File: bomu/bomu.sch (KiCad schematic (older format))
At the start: 19 parts, among them U1 NRF52840-CKAA-R7

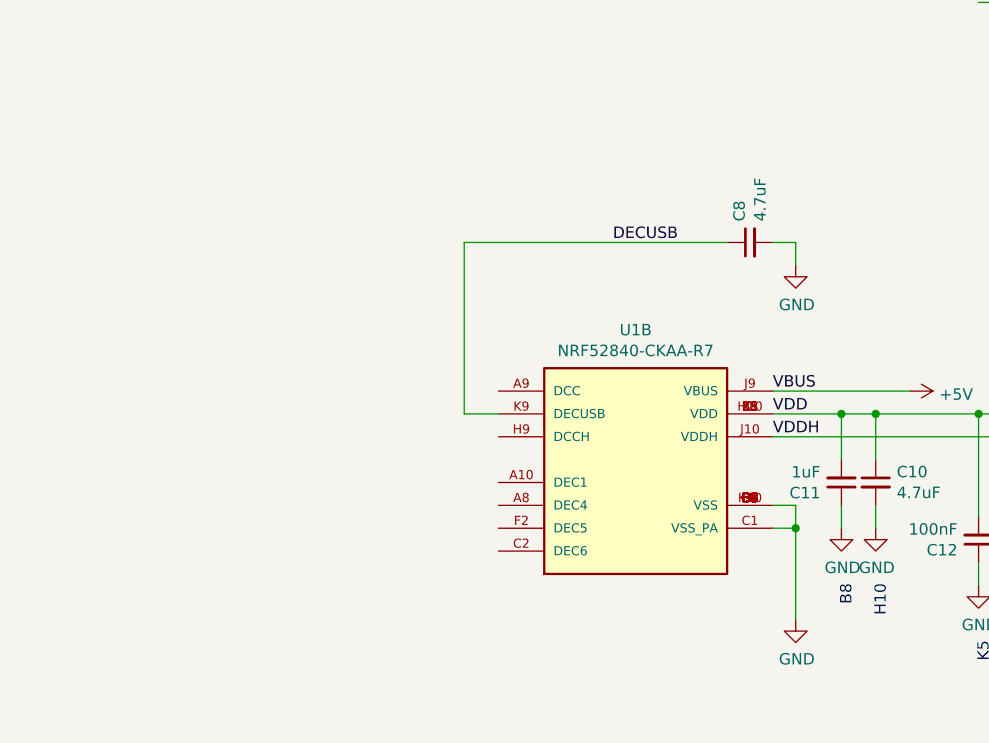
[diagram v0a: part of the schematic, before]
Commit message: Added remaining components to schematic
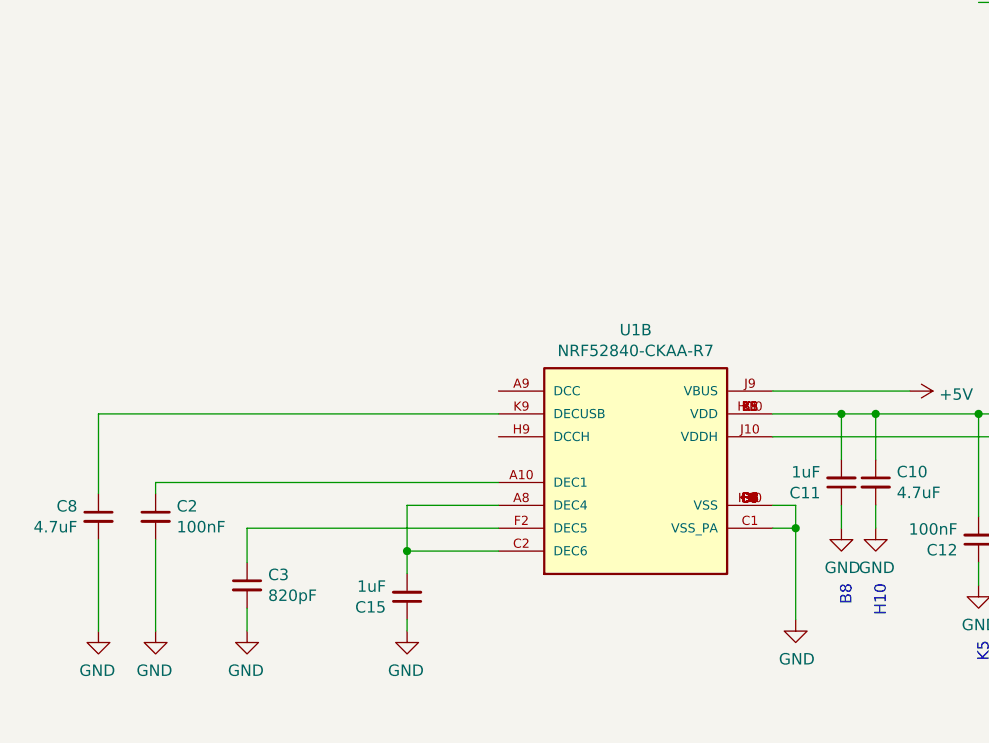
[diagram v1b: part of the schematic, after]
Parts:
- added C15: 1uF, Capacitor_SMD:C_0201_0603Metric, symbol Device:C_Small
- added C2: 100nF, Capacitor_SMD:C_0201_0603Metric, symbol Device:C_Small
- added C3: 820pF, Capacitor_SMD:C_0201_0603Metric, symbol Device:C_Small
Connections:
- net +5V: no longer R1.1
- net GND: now also C15.1, C2.2, C3.2
- net at U1.A10 (DEC1): now also C2.1
- net at U1.A8 (DEC4): now also U1.C2 (DEC6), C15.2
- net at U1.F2 (DEC5): now also C3.1
- net DECUSB: no longer names the net of C8.1, U1.K9 (DECUSB)
- new net VBUS: R1.1
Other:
- moved on the sheet: C8
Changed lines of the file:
@@
 	0    1    1    0
 $EndComp
-Text Label 3800 6300 0    50   ~ 0
-VBUS
-Text Label 3800 6400 0    50   ~ 0
-VDD
 $Comp
 L power:+3V0 #PWR?
@@
 	-1   0    0    1
 $EndComp
-Text Label 3800 6500 0    50   ~ 0
-VDDH
 $Comp
 L Device:R_Small_US R1
@@
 Wire Wire Line
 	3800 6400 4100 6400
-Text Label 3100 5650 0    50   ~ 0
-DECUSB
-$Comp
-L Device:C_Small C8
-U 1 1 5FCE36A5
-P 3700 5650
-F 0 "C8" H 3792 5696 50  0000 L CNN
-F 1 "4.7uF" H 3792 5605 50  0000 L CNN
-F 2 "Capacitor_SMD:C_0201_0603Metric" H 3700 5650 50  0001 C CNN
-F 3 "~" H 3700 5650 50  0001 C CNN
-	1    3700 5650
-	0    -1   -1   0
-$EndComp
-Wire Wire Line
-	3800 5650 3900 5650
-Wire Wire Line
-	3900 5650 3900 5750
 $Comp
 L power:GND #PWR?
 U 1 1 5FCE4C22
-P 3900 5750
-F 0 "#PWR?" H 3900 5500 50  0001 C CNN
-F 1 "GND" H 3905 5577 50  0000 C CNN
-F 2 "" H 3900 5750 50  0001 C CNN
-F 3 "" H 3900 5750 50  0001 C CNN
-	1    3900 5750
-	1    0    0    -1
-$EndComp
-Wire Wire Line
-	2600 6400 2450 6400
-Wire Wire Line
-	2450 6400 2450 5650
-Wire Wire Line
-	2450 5650 3600 5650
+P 850 7350
+F 0 "#PWR?" H 850 7100 50  0001 C CNN
+F 1 "GND" H 855 7177 50  0000 C CNN
+F 2 "" H 850 7350 50  0001 C CNN
+F 3 "" H 850 7350 50  0001 C CNN
+	1    850  7350
+	-1   0    0    -1
+$EndComp
 $Comp
 L Device:C_Small C10
@@
 Wire Wire Line
 	4150 2800 5100 2800
+$Comp
+L Device:C_Small C2
+U 1 1 5FE2FA10
+P 1100 6850
+F 0 "C2" H 1192 6896 50  0000 L CNN
+F 1 "100nF" H 1192 6805 50  0000 L CNN
+F 2 "Capacitor_SMD:C_0201_0603Metric" H 1100 6850 50  0001 C CNN
+F 3 "~" H 1100 6850 50  0001 C CNN
+	1    1100 6850
+	1    0    0    -1
+$EndComp
+$Comp
+L power:GND #PWR?
+U 1 1 5FE31818
+P 1100 7350
+F 0 "#PWR?" H 1100 7100 50  0001 C CNN
+F 1 "GND" H 1105 7177 50  0000 C CNN
+F 2 "" H 1100 7350 50  0001 C CNN
+F 3 "" H 1100 7350 50  0001 C CNN
+	1    1100 7350
+	-1   0    0    -1
+$EndComp
+Wire Wire Line
+	1100 7350 1100 6950
+Wire Wire Line
+	1100 6750 1100 6700
+Wire Wire Line
+	1100 6700 2600 6700
+$Comp
+L Device:C_Small C3
+U 1 1 5FE3522F
+P 1500 7150
+F 0 "C3" H 1592 7196 50  0000 L CNN
+F 1 "820pF" H 1592 7105 50  0000 L CNN
+F 2 "Capacitor_SMD:C_0201_0603Metric" H 1500 7150 50  0001 C CNN
+F 3 "~" H 1500 7150 50  0001 C CNN
+	1    1500 7150
+	1    0    0    -1
+$EndComp
+Wire Wire Line
+	2600 6900 1500 6900
+Wire Wire Line
+	1500 6900 1500 7050
+$Comp
+L power:GND #PWR?
+U 1 1 5FE3E73C
+P 1500 7350
+F 0 "#PWR?" H 1500 7100 50  0001 C CNN
+F 1 "GND" H 1505 7177 50  0000 C CNN
+F 2 "" H 1500 7350 50  0001 C CNN
+F 3 "" H 1500 7350 50  0001 C CNN
+	1    1500 7350
+	-1   0    0    -1
+$EndComp
+Wire Wire Line
+	1500 7250 1500 7350
+Wire Wire Line
+	2600 6800 2200 6800
+Wire Wire Line
+	2200 6800 2200 7000
+Wire Wire Line
+	2200 7000 2600 7000
+$Comp
+L Device:C_Small C15
+U 1 1 5FE428CE
+P 2200 7200
+F 0 "C15" H 2292 7246 50  0000 L CNN
+F 1 "1uF" H 2292 7155 50  0000 L CNN
+F 2 "Capacitor_SMD:C_0201_0603Metric" H 2200 7200 50  0001 C CNN
+F 3 "~" H 2200 7200 50  0001 C CNN
+	1    2200 7200
+	-1   0    0    1
+$EndComp
+Wire Wire Line
+	2200 7000 2200 7100
+Connection ~ 2200 7000
+$Comp
+L power:GND #PWR?
+U 1 1 5FE44CD1
+P 2200 7350
+F 0 "#PWR?" H 2200 7100 50  0001 C CNN
+F 1 "GND" H 2205 7177 50  0000 C CNN
+F 2 "" H 2200 7350 50  0001 C CNN
+F 3 "" H 2200 7350 50  0001 C CNN
+	1    2200 7350
+	-1   0    0    -1
+$EndComp
+Wire Wire Line
+	2200 7300 2200 7350
+$Comp
+L Device:C_Small C8
+U 1 1 5FCE36A5
+P 850 6850
+F 0 "C8" H 942 6896 50  0000 L CNN
+F 1 "4.7uF" H 942 6805 50  0000 L CNN
+F 2 "Capacitor_SMD:C_0201_0603Metric" H 850 6850 50  0001 C CNN
+F 3 "~" H 850 6850 50  0001 C CNN
+	1    850  6850
+	-1   0    0    -1
+$EndComp
+Wire Wire Line
+	850  6400 850  6750
+Wire Wire Line
+	850  6400 2600 6400
+Wire Wire Line
+	850  6950 850  7350
 $EndSCHEMATC

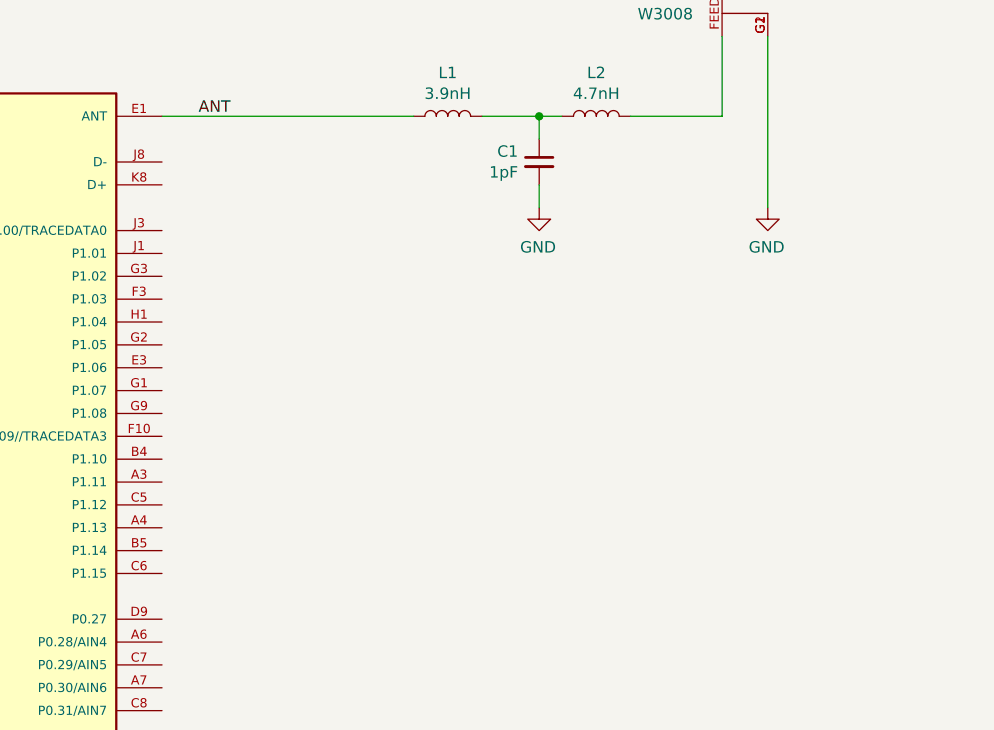
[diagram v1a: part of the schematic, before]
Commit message: Adding USB symbol. Will need custom USB A tab footprint
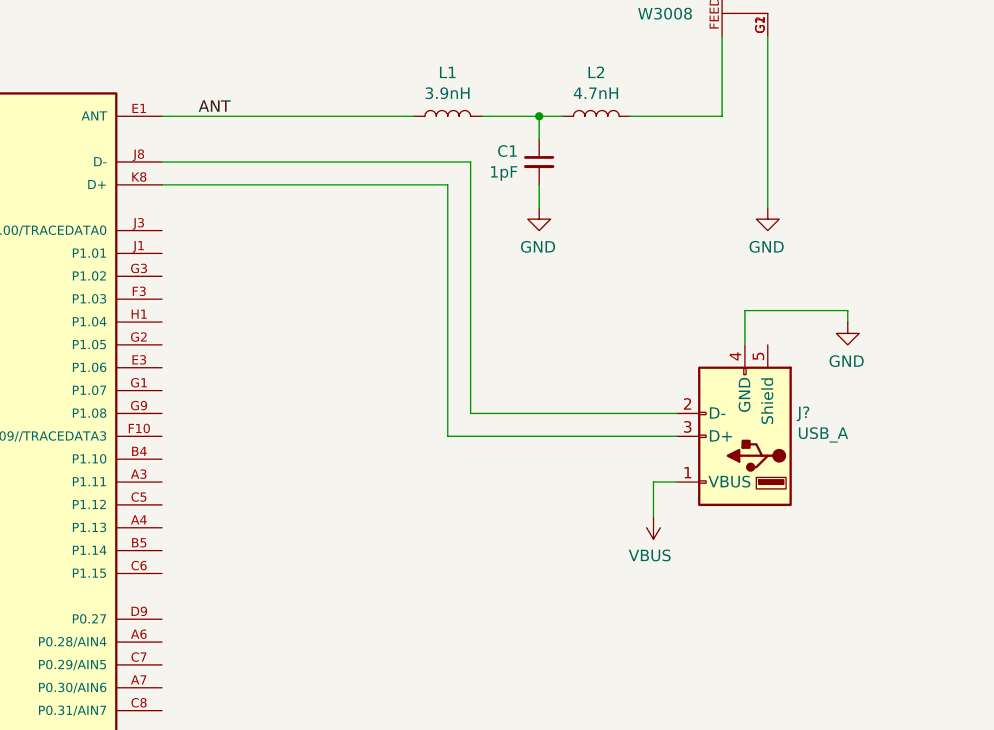
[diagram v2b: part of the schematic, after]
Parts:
- added J?: USB_A, symbol Connector:USB_A
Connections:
- net GND: now also J?.4 (GND)
- net VBUS: now also J?.1 (VBUS)
- net at U1.J8 (D-): now also J?.2 (D-)
- net at U1.K8 (D+): now also J?.3 (D+)
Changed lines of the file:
@@
 Wire Wire Line
 	850  6950 850  7350
+$Comp
+L Connector:USB_A J?
+U 1 1 5FCD2351
+P 9850 4200
+F 0 "J?" H 9620 4097 50  0000 R CNN
+F 1 "USB_A" H 9620 4188 50  0000 R CNN
+F 2 "" H 10000 4150 50  0001 C CNN
+F 3 " ~" H 10000 4150 50  0001 C CNN
+	1    9850 4200
+	-1   0    0    1
+$EndComp
+Wire Wire Line
+	7300 3000 8650 3000
+Wire Wire Line
+	8650 3000 8650 4100
+Wire Wire Line
+	8650 4100 9550 4100
+Wire Wire Line
+	7300 3100 8550 3100
+Wire Wire Line
+	8550 3100 8550 4200
+Wire Wire Line
+	8550 4200 9550 4200
+$Comp
+L power:GND #PWR?
+U 1 1 5FCDC106
+P 10300 3700
+F 0 "#PWR?" H 10300 3450 50  0001 C CNN
+F 1 "GND" H 10305 3527 50  0000 C CNN
+F 2 "" H 10300 3700 50  0001 C CNN
+F 3 "" H 10300 3700 50  0001 C CNN
+	1    10300 3700
+	-1   0    0    -1
+$EndComp
+Wire Wire Line
+	9850 3800 9850 3650
+Wire Wire Line
+	9850 3650 10300 3650
+Wire Wire Line
+	10300 3650 10300 3700
+$Comp
+L power:VBUS #PWR?
+U 1 1 5FCDF4FD
+P 9450 4550
+F 0 "#PWR?" H 9450 4400 50  0001 C CNN
+F 1 "VBUS" H 9465 4723 50  0000 C CNN
+F 2 "" H 9450 4550 50  0001 C CNN
+F 3 "" H 9450 4550 50  0001 C CNN
+	1    9450 4550
+	-1   0    0    1
+$EndComp
+Wire Wire Line
+	9550 4400 9450 4400
+Wire Wire Line
+	9450 4400 9450 4550
 $EndSCHEMATC

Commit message: Updating schematic info
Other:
- note added: "Using datasheet figure 216: Circuit configuration no. 1 schematic for CKAA WLCSP"
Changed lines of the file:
@@
 Wire Wire Line
 	9450 4400 9450 4550
+Text Notes 7050 6650 0    50   ~ 0
+Using datasheet figure 216: Circuit configuration no. 1 schematic for CKAA WLCSP
 $EndSCHEMATC

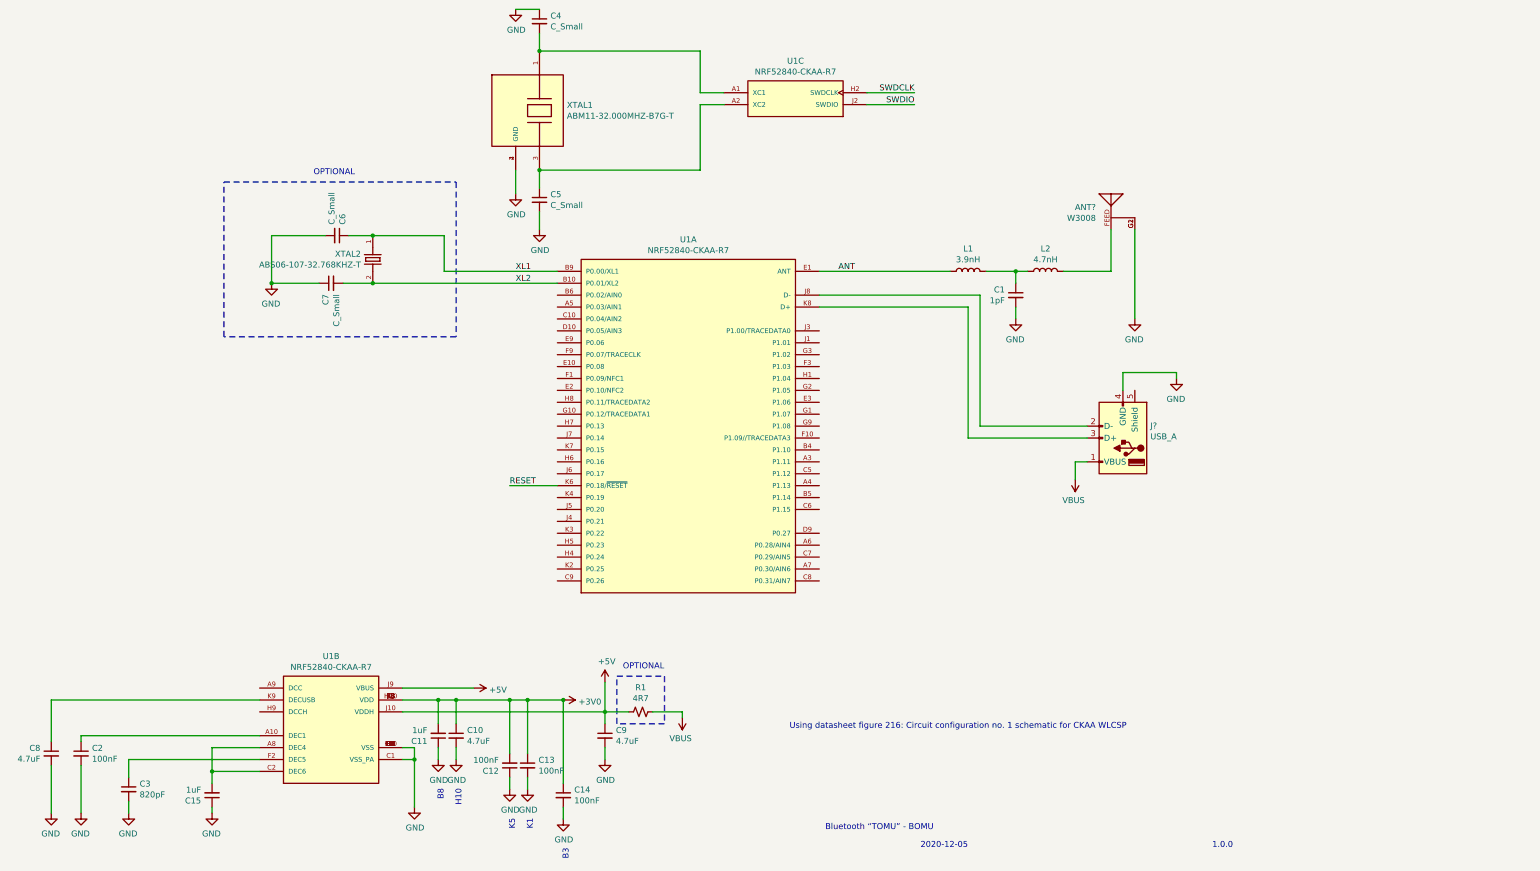
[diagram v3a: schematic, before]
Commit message: Adding custom USB A tab insert symbol and footprint. Started work on PCB
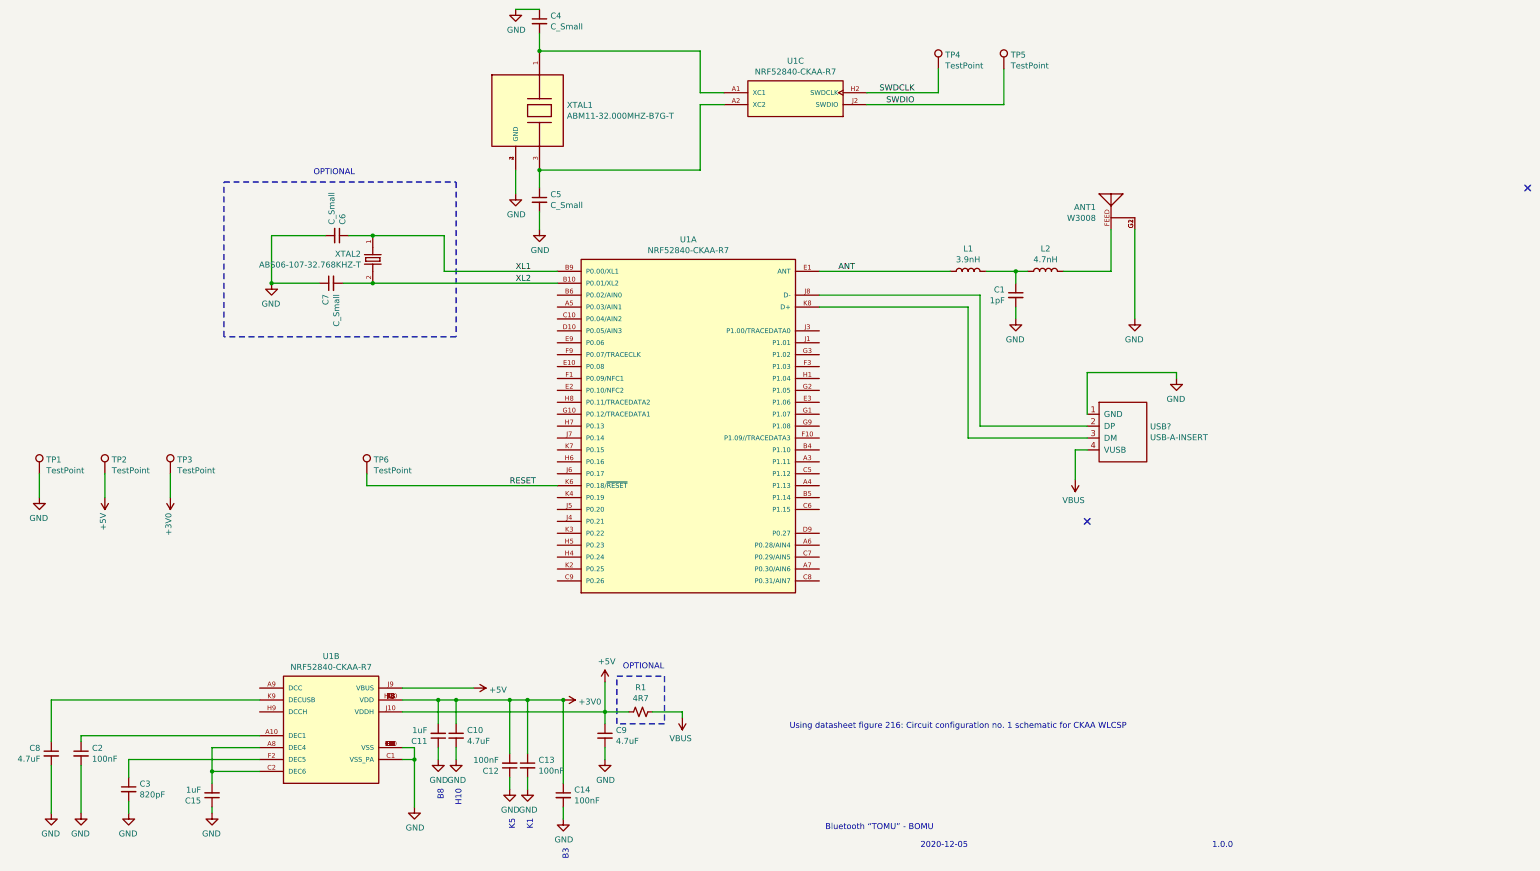
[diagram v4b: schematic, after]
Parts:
- removed J?: USB_A, symbol Connector:USB_A
- added TP1, TP2, TP3, TP4, TP5, TP6: TestPoint, TestPoint:TestPoint_Pad_D1.0mm, symbol Connector:TestPoint
- added USB?: USB-A-INSERT, bomu-usb-a-insert:USB_A_SOCKET_PCB_INSERT, symbol bomu-usb-a-insert:USB-A-INSERT
- ANT1: renamed from ANT?; footprint ANTENNA_W3008 -> W3008:ANTENNA_W3008
- U1: footprint BGA94N35P10X10_360X354X51N -> NRF52840-CKAA-R7:BGA94N35P10X10_360X354X51N
- XTAL1: footprint OSCCC200X160X59 -> ABM11-32:OSCCC200X160X59
- XTAL2: footprint XTAL_ABS06-107-32.768KHZ-T -> ABS06-107-32:XTAL_ABS06-107-32.768KHZ-T
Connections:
- net +3V0: now also TP3.1
- net +5V: now also TP2.1
- net GND: now also TP1.1, USB?.1 (GND)
- net RESET: now also TP6.1
- net SWDCLK: now also TP4.1
- net SWDIO: now also TP5.1
- net VBUS: now also USB?.4 (VUSB)
- net at U1.J8 (D-): now also USB?.2 (DP)
- net at U1.K8 (D+): now also USB?.3 (DM)
- no-connect marks 0 -> 2

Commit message: Current work on the PCB
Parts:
- gave numbers to parts that had none: 1
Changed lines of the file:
@@
 NoConn ~ 9550 4900
 $Comp
-L bomu-usb-a-insert:USB-A-INSERT USB?
+L bomu-usb-a-insert:USB-A-INSERT USB1
 U 1 1 5FD36893
 P 9550 3900
-F 0 "USB?" H 9022 3696 50  0000 R CNN
+F 0 "USB1" H 9022 3696 50  0000 R CNN
 F 1 "USB-A-INSERT" H 9022 3605 50  0000 R CNN
 F 2 "bomu-usb-a-insert:USB_A_SOCKET_PCB_INSERT" H 9550 3900 50  0001 C CNN
